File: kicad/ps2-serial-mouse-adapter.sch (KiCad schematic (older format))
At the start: 11 parts, among them U1 Arduino_Mini, U2 MAX232

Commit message: Add necroware kicad library
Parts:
- MOUSE1: footprint MyLibrary:Mini_DIN_6_LCSC_C77848 -> Necroware:Mini_DIN_6_LCSC_C77848; symbol MyLib:Mini-DIN-6_shielded -> Necroware:Mini-DIN-6_shielded
- U1: symbol MyLib:Arduino_Mini -> Necroware:Arduino_Mini
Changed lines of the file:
@@
 NoConn ~ 3200 4250
 $Comp
-L MyLib:Arduino_Mini U1
+L Necroware:Arduino_Mini U1
 U 1 1 5FBA0BED
 P 3200 2950
@@
 $EndComp
 $Comp
-L MyLib:Mini-DIN-6_shielded MOUSE1
+L Necroware:Mini-DIN-6_shielded MOUSE1
 U 1 1 5FBA6BF7
 P 3550 2400
 F 0 "MOUSE1" H 3550 2767 50  0000 C CNN
 F 1 "Mini-DIN-6" H 3550 2676 50  0000 C CNN
-F 2 "MyLibrary:Mini_DIN_6_LCSC_C77848" H 3550 2400 50  0001 C CNN
+F 2 "Necroware:Mini_DIN_6_LCSC_C77848" H 3550 2400 50  0001 C CNN
 F 3 "http://service.powerdynamics.com/ec/Catalog17/Section%2011.pdf" H 3550 2400 50  0001 C CNN
 F 4 "C77848" H 3550 2400 50  0001 C CNN "LCSC"

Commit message: Update LSCS part number
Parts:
- MOUSE1: LCSC C77848 -> (none); LCSC Part (none) -> C77848
- U2: LCSC Part (none) -> C911187
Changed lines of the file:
@@
 F 2 "Package_DIP:DIP-16_W7.62mm_Socket" H 6350 2650 50  0001 L CNN
 F 3 "http://www.ti.com/lit/ds/symlink/max232.pdf" H 6300 3800 50  0001 C CNN
+F 4 "C911187" H 6300 3700 50  0001 C CNN "LCSC Part"
 	1    6300 3700
 	1    0    0    -1
@@
 F 2 "Necroware:Mini_DIN_6_LCSC_C77848" H 3550 2400 50  0001 C CNN
 F 3 "http://service.powerdynamics.com/ec/Catalog17/Section%2011.pdf" H 3550 2400 50  0001 C CNN
-F 4 "C77848" H 3550 2400 50  0001 C CNN "LCSC"
+F 4 "C77848" H 3550 2400 50  0001 C CNN "LCSC Part"
 	1    3550 2400
 	-1   0    0    1

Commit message: Replace DB9 by DB9_mounting_holes
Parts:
- RS232: symbol Connector:DB9_Female -> Connector:DB9_Female_MountingHoles
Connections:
- wire segments 27 -> 29
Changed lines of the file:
@@
 NoConn ~ 7900 4300
 $Comp
-L Connector:DB9_Female RS232
+L Connector:DB9_Female_MountingHoles RS232
 U 1 1 5FBA566F
 P 8200 4000
@@
 L power:GND #PWR07
 U 1 1 5FB93712
-P 7900 4400
-F 0 "#PWR07" H 7900 4150 50  0001 C CNN
-F 1 "GND" H 7900 4250 50  0000 C CNN
-F 2 "" H 7900 4400 50  0001 C CNN
-F 3 "" H 7900 4400 50  0001 C CNN
-	1    7900 4400
+P 8200 4600
+F 0 "#PWR07" H 8200 4350 50  0001 C CNN
+F 1 "GND" H 8200 4450 50  0000 C CNN
+F 2 "" H 8200 4600 50  0001 C CNN
+F 3 "" H 8200 4600 50  0001 C CNN
+	1    8200 4600
 	1    0    0    -1
 $EndComp
@@
 $EndComp
 Connection ~ 4800 4150
+Wire Wire Line
+	7900 4400 7900 4600
+Wire Wire Line
+	7900 4600 8200 4600
+Connection ~ 8200 4600
 $EndSCHEMATC

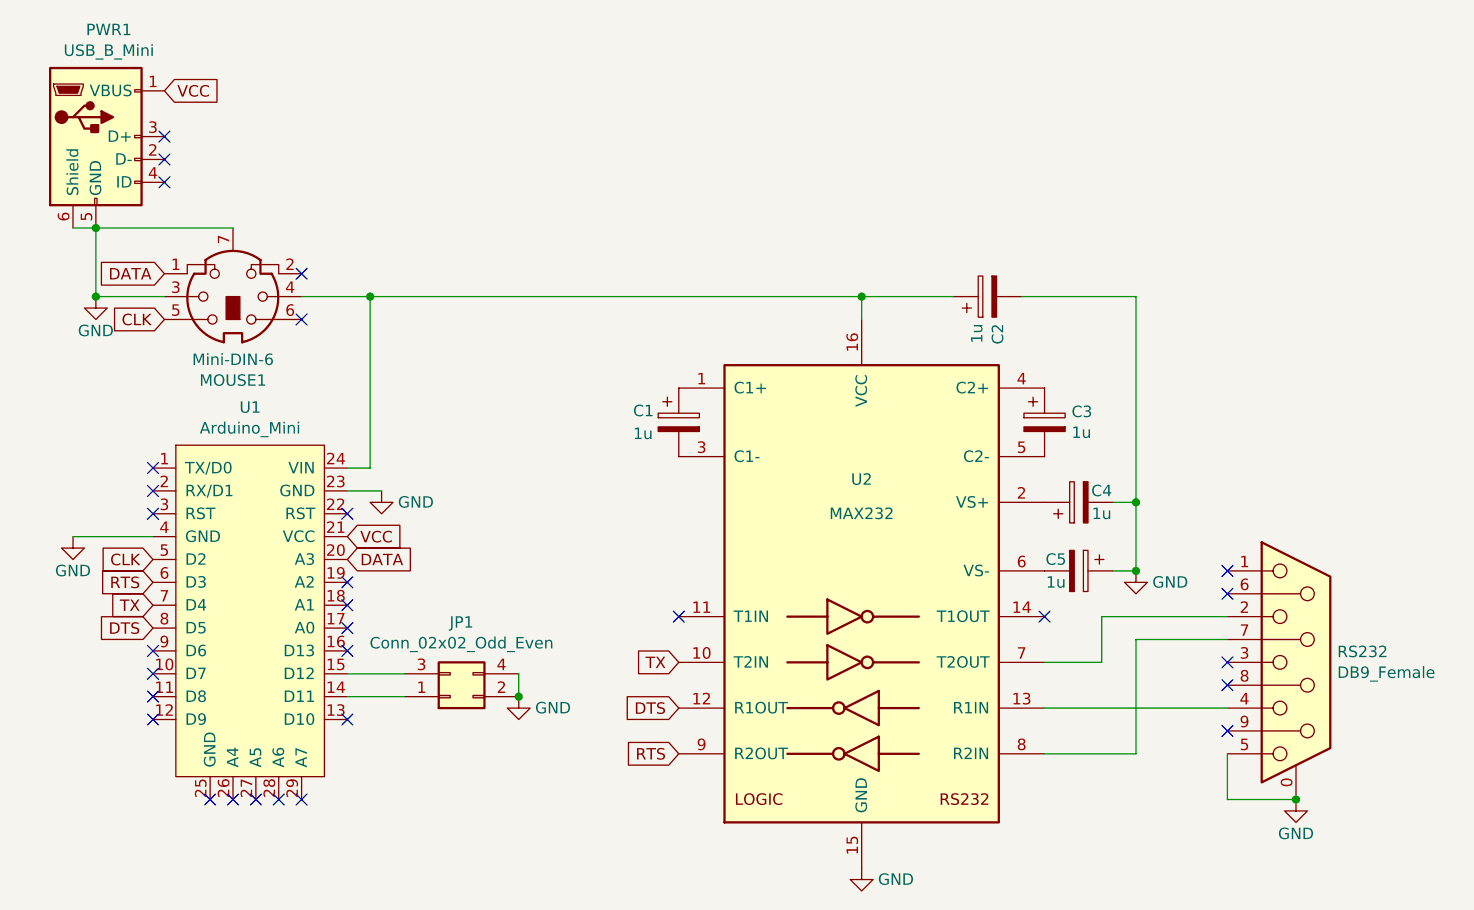
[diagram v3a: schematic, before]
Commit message: Fix wrong VCC network
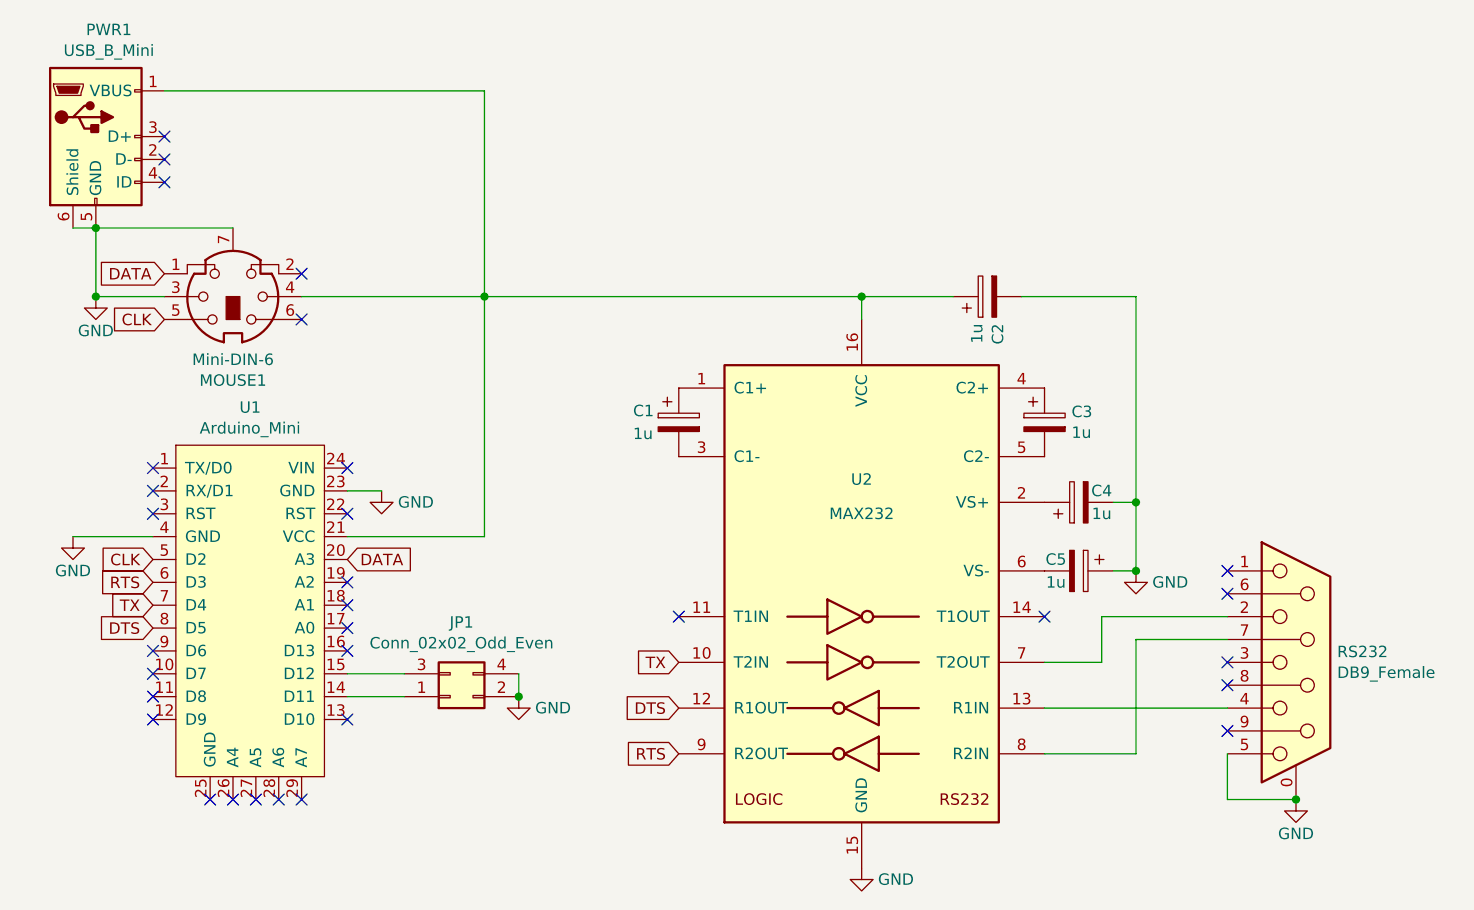
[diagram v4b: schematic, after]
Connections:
- net VCC is gone; now on an unnamed net: PWR1.1 (VBUS), U1.21 (VCC)
- net at C2.1, MOUSE1.4, U2.16 (VCC): no longer U1.24 (VIN)
- no-connect marks 30 -> 31
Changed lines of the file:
@@
 Sheet 1 1
 Title "PS/2 to Serial Mouse Adapter"
-Date "2020-11-21"
-Rev "0.5"
+Date "2020-12-08"
+Rev "0.6"
 Comp "Necroware"
 Comment1 "by Scorp"
@@
 Wire Wire Line
 	6300 2400 6300 2500
-Wire Wire Line
-	4050 3150 4150 3150
-Wire Wire Line
-	4150 3150 4150 2400
-Wire Wire Line
-	4150 2400 6300 2400
 Connection ~ 6300 2400
 NoConn ~ 3200 3150
@@
 NoConn ~ 4050 3950
 NoConn ~ 4050 4250
-Text GLabel 4050 3450 2    50   Input ~ 0
-VCC
 NoConn ~ 3550 4600
 NoConn ~ 3650 4600
@@
 Text GLabel 3250 2300 0    50   Input ~ 0
 DATA
-Wire Wire Line
-	3850 2400 4150 2400
-Connection ~ 4150 2400
 Text GLabel 3200 3550 0    50   Input ~ 0
 CLK
@@
 	1    0    0    -1
 $EndComp
-Text GLabel 3250 1500 2    50   Input ~ 0
-VCC
 NoConn ~ 3250 1700
 NoConn ~ 3250 1800
@@
 NoConn ~ 3200 4150
 NoConn ~ 3200 4250
-$Comp
-L Necroware:Arduino_Mini U1
-U 1 1 5FBA0BED
-P 3200 2950
-F 0 "U1" H 3625 3015 50  0000 C CNN
-F 1 "Arduino_Mini" H 3625 2924 50  0000 C CNN
-F 2 "Package_DIP:DIP-24_W15.24mm_Socket" H 3200 2950 50  0001 C CNN
-F 3 "" H 3200 2950 50  0001 C CNN
-	1    3200 2950
-	1    0    0    -1
-$EndComp
 $Comp
 L Necroware:Mini-DIN-6_shielded MOUSE1
@@
 	7900 4600 8200 4600
 Connection ~ 8200 4600
+$Comp
+L Necroware:Arduino_Mini U1
+U 1 1 5FBA0BED
+P 3200 2950
+F 0 "U1" H 3625 3015 50  0000 C CNN
+F 1 "Arduino_Mini" H 3625 2924 50  0000 C CNN
+F 2 "Package_DIP:DIP-24_W15.24mm_Socket" H 3200 2950 50  0001 C CNN
+F 3 "" H 3200 2950 50  0001 C CNN
+	1    3200 2950
+	1    0    0    -1
+$EndComp
+Wire Wire Line
+	3850 2400 4650 2400
+NoConn ~ 4050 3150
+Wire Wire Line
+	4050 3450 4650 3450
+Wire Wire Line
+	4650 3450 4650 2400
+Connection ~ 4650 2400
+Wire Wire Line
+	4650 2400 6300 2400
+Wire Wire Line
+	3250 1500 4650 1500
+Wire Wire Line
+	4650 1500 4650 2400
 $EndSCHEMATC

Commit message: Replace serial DTR through TX.
DTR was not used anyway and TX can be used in the future for
communication with the adapter through serial port
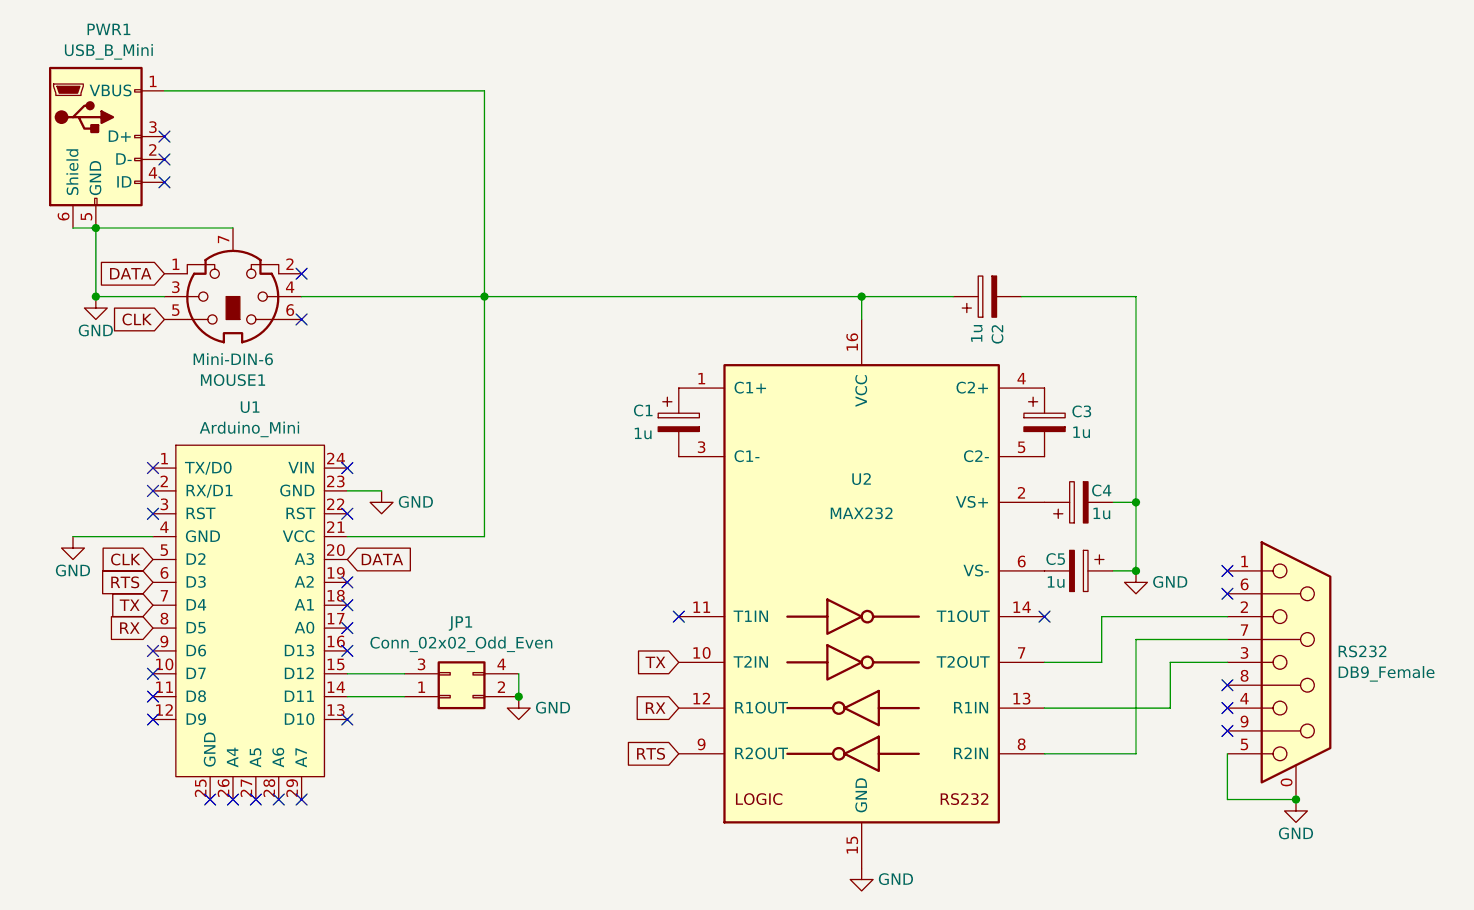
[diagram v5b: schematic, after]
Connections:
- net at U2.13 (R1IN): now also RS232.3; no longer RS232.4
- net DTS renamed RX
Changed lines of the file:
@@
 NoConn ~ 7900 4300
-$Comp
-L Connector:DB9_Female_MountingHoles RS232
-U 1 1 5FBA566F
-P 8200 4000
-F 0 "RS232" H 8380 4046 50  0000 L CNN
-F 1 "DB9_Female" H 8380 3955 50  0000 L CNN
-F 2 "Connector_Dsub:DSUB-9_Female_Horizontal_P2.77x2.84mm_EdgePinOffset7.70mm_Housed_MountingHolesOffset9.12mm" H 8200 4000 50  0001 C CNN
-F 3 " ~" H 8200 4000 50  0001 C CNN
-	1    8200 4000
-	1    0    0    -1
-$EndComp
 $Comp
 L power:GND #PWR07
@@
 	1    0    0    -1
 $EndComp
-NoConn ~ 7900 4000
 Text GLabel 5500 4000 0    50   Input ~ 0
 TX
 Text GLabel 5500 4400 0    50   Input ~ 0
 RTS
-Text GLabel 5500 4200 0    50   Input ~ 0
-DTS
 Wire Wire Line
 	7500 4400 7500 3900
@@
 TX
 Text GLabel 3200 3850 0    50   Input ~ 0
-DTS
-Wire Wire Line
-	7100 4200 7900 4200
+RX
+Wire Wire Line
+	7100 4200 7650 4200
 Wire Wire Line
 	7500 4400 7100 4400
@@
 Wire Wire Line
 	7900 4600 8200 4600
-Connection ~ 8200 4600
 $Comp
 L Necroware:Arduino_Mini U1
@@
 Wire Wire Line
 	4650 1500 4650 2400
+Wire Wire Line
+	7650 4200 7650 4000
+Wire Wire Line
+	7650 4000 7900 4000
+Connection ~ 8200 4600
+$Comp
+L Connector:DB9_Female_MountingHoles RS232
+U 1 1 5FBA566F
+P 8200 4000
+F 0 "RS232" H 8380 4046 50  0000 L CNN
+F 1 "DB9_Female" H 8380 3955 50  0000 L CNN
+F 2 "Connector_Dsub:DSUB-9_Female_Horizontal_P2.77x2.84mm_EdgePinOffset7.70mm_Housed_MountingHolesOffset9.12mm" H 8200 4000 50  0001 C CNN
+F 3 " ~" H 8200 4000 50  0001 C CNN
+	1    8200 4000
+	1    0    0    -1
+$EndComp
+NoConn ~ 7900 4200
+Text GLabel 5500 4200 0    50   Input ~ 0
+RX
 $EndSCHEMATC

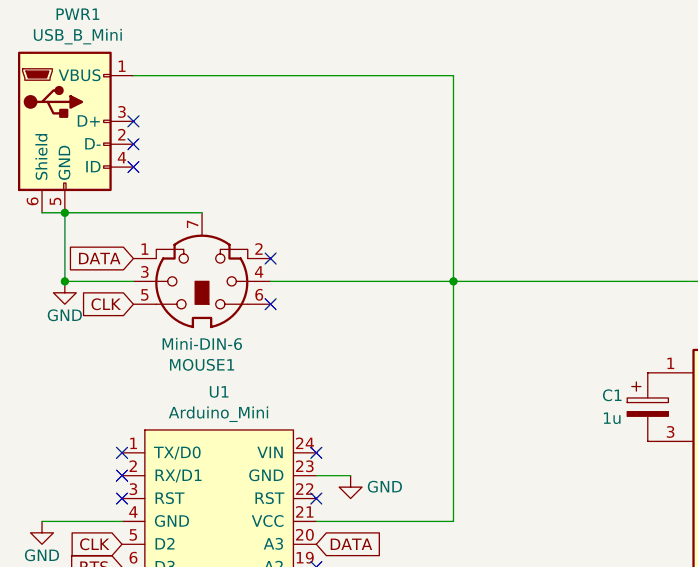
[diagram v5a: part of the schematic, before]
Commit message: Add a pull-up resistor to the ps/2 clock
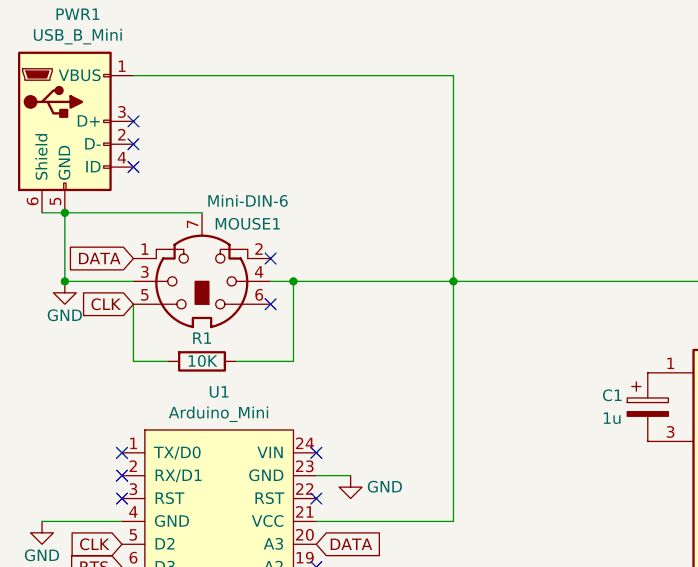
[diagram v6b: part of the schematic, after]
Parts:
- added R1: 10K, Resistor_THT:R_Axial_DIN0207_L6.3mm_D2.5mm_P7.62mm_Horizontal, symbol Device:R
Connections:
- net CLK: now also R1.2
- net at C2.1, MOUSE1.4, PWR1.1 (VBUS)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: now also R1.1
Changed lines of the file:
@@
 Sheet 1 1
 Title "PS/2 to Serial Mouse Adapter"
-Date "2020-12-08"
-Rev "0.6"
+Date "2021-10-22"
+Rev "0.7"
 Comp "Necroware"
 Comment1 "by Scorp"
@@
 NoConn ~ 3200 4150
 NoConn ~ 3200 4250
-$Comp
-L Necroware:Mini-DIN-6_shielded MOUSE1
-U 1 1 5FBA6BF7
-P 3550 2400
-F 0 "MOUSE1" H 3550 2767 50  0000 C CNN
-F 1 "Mini-DIN-6" H 3550 2676 50  0000 C CNN
-F 2 "Necroware:Mini_DIN_6_LCSC_C77848" H 3550 2400 50  0001 C CNN
-F 3 "http://service.powerdynamics.com/ec/Catalog17/Section%2011.pdf" H 3550 2400 50  0001 C CNN
-F 4 "C77848" H 3550 2400 50  0001 C CNN "LCSC Part"
-	1    3550 2400
-	-1   0    0    1
-$EndComp
 Wire Wire Line
 	2950 2100 3550 2100
@@
 $EndComp
 Wire Wire Line
-	3850 2400 4650 2400
+	3850 2400 3950 2400
 NoConn ~ 4050 3150
 Wire Wire Line
@@
 Text GLabel 5500 4200 0    50   Input ~ 0
 RX
+$Comp
+L Device:R R1
+U 1 1 6172B4AF
+P 3550 2750
+F 0 "R1" V 3450 2750 50  0000 C CNN
+F 1 "10K" V 3550 2750 50  0000 C CNN
+F 2 "Resistor_THT:R_Axial_DIN0207_L6.3mm_D2.5mm_P7.62mm_Horizontal" V 3480 2750 50  0001 C CNN
+F 3 "~" H 3550 2750 50  0001 C CNN
+	1    3550 2750
+	0    1    1    0
+$EndComp
+$Comp
+L Necroware:Mini-DIN-6_shielded MOUSE1
+U 1 1 5FBA6BF7
+P 3550 2400
+F 0 "MOUSE1" H 3350 2150 50  0000 C CNN
+F 1 "Mini-DIN-6" H 3350 2050 50  0000 C CNN
+F 2 "Necroware:Mini_DIN_6_LCSC_C77848" H 3550 2400 50  0001 C CNN
+F 3 "http://service.powerdynamics.com/ec/Catalog17/Section%2011.pdf" H 3550 2400 50  0001 C CNN
+F 4 "C77848" H 3550 2400 50  0001 C CNN "LCSC Part"
+	1    3550 2400
+	-1   0    0    1
+$EndComp
+Wire Wire Line
+	3250 2500 3250 2750
+Wire Wire Line
+	3250 2750 3400 2750
+Wire Wire Line
+	3700 2750 3950 2750
+Wire Wire Line
+	3950 2750 3950 2400
+Connection ~ 3950 2400
+Wire Wire Line
+	3950 2400 4650 2400
 $EndSCHEMATC

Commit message: Added LCSC part number for R1
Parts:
- R1: LCSC (none) -> C57436
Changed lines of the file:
@@
 F 2 "Resistor_THT:R_Axial_DIN0207_L6.3mm_D2.5mm_P7.62mm_Horizontal" V 3480 2750 50  0001 C CNN
 F 3 "~" H 3550 2750 50  0001 C CNN
+F 4 "C57436" V 3550 2750 50  0001 C CNN "LCSC"
 	1    3550 2750
 	0    1    1    0
